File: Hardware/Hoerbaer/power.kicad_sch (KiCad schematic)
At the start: 62 parts, among them J12 Battery 1S Li-Ion, Q1 DMG3415UQ-7, U12 MAX17048G, U13 TPS61288, U8 MCP73831T-2ACI/OT (4.2V), U9 TPS63001

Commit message: Many small corrections, changed connectors, ...
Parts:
- added J10: Battery 1S Li-Ion, Connector_Wire:SolderWire-0.5sqmm_1x02_P4.6mm_D0.9mm_OD2.1mm, symbol Connector_Generic:Conn_01x02
- J12: footprint Connector_Phoenix_MSTB:PhoenixContact_MSTBVA_2,5_2-G-5,08_1x02_P5.08mm_Vertical -> Connector_JST:JST_XH_B2B-XH-AM_1x02_P2.50mm_Vertical; LCSC (none) -> C158012; MPN (none) -> B2B-XH-A(LF)(SN); now not fitted
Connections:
- net +BATT: now also J10.2 (Pin_2)
- net GND: now also J10.1 (Pin_1)
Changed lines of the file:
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@@
   (junction (at 191.77 142.24) (diameter 0) (color 0 0 0 0)
   )
+  (junction (at 237.49 139.7) (diameter 0) (color 0 0 0 0)
+  )
   (junction (at 107.95 43.18) (diameter 0) (color 0 0 0 0)
   )
@@
     (stroke (width 0) (type default))
   )
+  (wire (pts (xy 237.49 139.7) (xy 237.49 153.67))
+    (stroke (width 0) (type default))
+  )
   (wire (pts (xy 191.77 142.24) (xy 191.77 138.43))
     (stroke (width 0) (type default))
@@
     (stroke (width 0) (type default))
   )
+  (wire (pts (xy 237.49 153.67) (xy 245.11 153.67))
+    (stroke (width 0) (type default))
+  )
   (wire (pts (xy 199.39 142.24) (xy 199.39 146.05))
     (stroke (width 0) (type default))
@@
     )
   )
+  (symbol (lib_id "Connector_Generic:Conn_01x02") (at 250.19 156.21 0) (mirror x) (unit 1)
+    (in_bom no) (on_board yes) (dnp no)
+    (property "Reference" "J10" (at 252.73 156.21 0)
+      (effects (font (size 1.27 1.27)) (justify left))
+    )
+    (property "Value" "Battery 1S Li-Ion" (at 252.73 153.67 0)
+      (effects (font (size 1.27 1.27)) (justify left))
+    )
+    (property "Footprint" "Connector_Wire:SolderWire-0.5sqmm_1x02_P4.6mm_D0.9mm_OD2.1mm" (at 250.19 156.21 0)
+      (effects (font (size 1.27 1.27)) hide)
+    )
+    (property "Datasheet" "~" (at 250.19 156.21 0)
+      (effects (font (size 1.27 1.27)) hide)
+    )
+    (property "MPN" "" (at 250.19 156.21 0)
+      (effects (font (size 1.27 1.27)) hide)
+    )
+    (property "LCSC" "" (at 250.19 156.21 0)
+      (effects (font (size 1.27 1.27)) hide)
+    )
+    (property "Field6" "" (at 250.19 156.21 0)
+      (effects (font (size 1.27 1.27)) hide)
+    )
+    (pin "1")
+    (pin "2")
+    (instances
+      (project "Hoerbaer"
+        (path "/31f16f54-0469-45ae-b442-d363bf5fad3b/619abe22-66a2-4b7d-b472-86dccb0a4dd1"
+          (reference "J10") (unit 1)
+        )
+      )
+    )
+  )
   (symbol (lib_id "Connector:TestPoint") (at 181.61 43.18 270) (unit 1)
     (in_bom no) (on_board yes) (dnp no)
@@
     )
   )
+  (symbol (lib_id "power:GND") (at 245.11 156.21 0) (unit 1)
+    (in_bom yes) (on_board yes) (dnp no)
+    (property "Reference" "#PWR0193" (at 245.11 162.56 0)
+      (effects (font (size 1.27 1.27)) hide)
+    )
+    (property "Value" "GND" (at 245.11 160.02 0)
+      (effects (font (size 1.27 1.27)))
+    )
+    (property "Footprint" "" (at 245.11 156.21 0)
+      (effects (font (size 1.27 1.27)) hide)
+    )
+    (property "Datasheet" "" (at 245.11 156.21 0)
+      (effects (font (size 1.27 1.27)) hide)
+    )
+    (pin "1")
+    (instances
+      (project "Hoerbaer"
+        (path "/31f16f54-0469-45ae-b442-d363bf5fad3b/619abe22-66a2-4b7d-b472-86dccb0a4dd1"
+          (reference "#PWR0193") (unit 1)
+        )
+      )
+    )
+  )
   (symbol (lib_id "Baer_Symbols:MAX17048 DFN8") (at 247.65 102.87 0) (unit 1)
     (in_bom yes) (on_board yes) (dnp no) (fields_autoplaced)
@@
   )
   (symbol (lib_id "Connector_Generic:Conn_01x02") (at 250.19 142.24 0) (mirror x) (unit 1)
-    (in_bom yes) (on_board yes) (dnp no)
+    (in_bom yes) (on_board yes) (dnp yes)
     (property "Reference" "J12" (at 252.73 142.24 0)
       (effects (font (size 1.27 1.27)) (justify left))
@@
       (effects (font (size 1.27 1.27)) (justify left))
     )
-    (property "Footprint" "Connector_Phoenix_MSTB:PhoenixContact_MSTBVA_2,5_2-G-5,08_1x02_P5.08mm_Vertical" (at 250.19 142.24 0)
+    (property "Footprint" "Connector_JST:JST_XH_B2B-XH-AM_1x02_P2.50mm_Vertical" (at 250.19 142.24 0)
       (effects (font (size 1.27 1.27)) hide)
     )
@@
       (effects (font (size 1.27 1.27)) hide)
     )
+    (property "MPN" "B2B-XH-A(LF)(SN)" (at 250.19 142.24 0)
+      (effects (font (size 1.27 1.27)) hide)
+    )
+    (property "LCSC" "C158012" (at 250.19 142.24 0)
+      (effects (font (size 1.27 1.27)) hide)
+    )

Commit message: DRC fixes
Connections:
- net GND: now also NT1.1, NT10.1, NT11.1, NT12.1, NT13.1, NT14.1, NT2.1, NT3.1, NT4.1, NT5.1, NT6.1, NT7.1, NT8.1, NT9.1; no longer NT1.2, NT10.2, NT11.2, NT12.2, NT13.2, NT14.2, NT2.2, NT3.2, NT4.2, NT5.2, NT6.2, NT7.2, NT8.2, NT9.2
- net GNDPWR: now also NT1.2, NT10.2, NT11.2, NT12.2, NT13.2, NT14.2, NT2.2, NT3.2, NT4.2, NT5.2, NT6.2, NT7.2, NT8.2, NT9.2; no longer NT1.1, NT10.1, NT11.1, NT12.1, NT13.1, NT14.1, NT2.1, NT3.1, NT4.1, NT5.1, NT6.1, NT7.1, NT8.1, NT9.1
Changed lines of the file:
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@@
     )
   )
-  (symbol (lib_id "power:GNDPWR") (at 176.53 146.05 0) (unit 1)
+  (symbol (lib_id "power:GNDPWR") (at 184.15 146.05 0) (unit 1)
     (in_bom yes) (on_board yes) (dnp no) (fields_autoplaced)
-    (property "Reference" "#PWR0151" (at 176.53 151.13 0)
-      (effects (font (size 1.27 1.27)) hide)
-    )
-    (property "Value" "GNDPWR" (at 176.403 149.86 0)
-      (effects (font (size 1.27 1.27)))
-    )
-    (property "Footprint" "" (at 176.53 147.32 0)
-      (effects (font (size 1.27 1.27)) hide)
-    )
-    (property "Datasheet" "" (at 176.53 147.32 0)
+    (property "Reference" "#PWR0151" (at 184.15 151.13 0)
+      (effects (font (size 1.27 1.27)) hide)
+    )
+    (property "Value" "GNDPWR" (at 184.023 149.86 0)
+      (effects (font (size 1.27 1.27)))
+    )
+    (property "Footprint" "" (at 184.15 147.32 0)
+      (effects (font (size 1.27 1.27)) hide)
+    )
+    (property "Datasheet" "" (at 184.15 147.32 0)
       (effects (font (size 1.27 1.27)) hide)
     )
@@
     )
   )
-  (symbol (lib_id "power:GND") (at 184.15 146.05 0) (unit 1)
-    (in_bom yes) (on_board yes) (dnp no)
-    (property "Reference" "#PWR0152" (at 184.15 152.4 0)
-      (effects (font (size 1.27 1.27)) hide)
-    )
-    (property "Value" "GND" (at 184.15 149.86 0)
-      (effects (font (size 1.27 1.27)))
-    )
-    (property "Footprint" "" (at 184.15 146.05 0)
-      (effects (font (size 1.27 1.27)) hide)
-    )
-    (property "Datasheet" "" (at 184.15 146.05 0)
+  (symbol (lib_id "power:GND") (at 176.53 146.05 0) (unit 1)
+    (in_bom yes) (on_board yes) (dnp no)
+    (property "Reference" "#PWR0152" (at 176.53 152.4 0)
+      (effects (font (size 1.27 1.27)) hide)
+    )
+    (property "Value" "GND" (at 176.53 149.86 0)
+      (effects (font (size 1.27 1.27)))
+    )
+    (property "Footprint" "" (at 176.53 146.05 0)
+      (effects (font (size 1.27 1.27)) hide)
+    )
+    (property "Datasheet" "" (at 176.53 146.05 0)
       (effects (font (size 1.27 1.27)) hide)
     )
@@
     )
   )
-  (symbol (lib_id "power:GNDPWR") (at 191.77 146.05 0) (unit 1)
+  (symbol (lib_id "power:GNDPWR") (at 199.39 146.05 0) (unit 1)
     (in_bom yes) (on_board yes) (dnp no) (fields_autoplaced)
-    (property "Reference" "#PWR0190" (at 191.77 151.13 0)
-      (effects (font (size 1.27 1.27)) hide)
-    )
-    (property "Value" "GNDPWR" (at 191.643 149.86 0)
-      (effects (font (size 1.27 1.27)))
-    )
-    (property "Footprint" "" (at 191.77 147.32 0)
-      (effects (font (size 1.27 1.27)) hide)
-    )
-    (property "Datasheet" "" (at 191.77 147.32 0)
+    (property "Reference" "#PWR0190" (at 199.39 151.13 0)
+      (effects (font (size 1.27 1.27)) hide)
+    )
+    (property "Value" "GNDPWR" (at 199.263 149.86 0)
+      (effects (font (size 1.27 1.27)))
+    )
+    (property "Footprint" "" (at 199.39 147.32 0)
+      (effects (font (size 1.27 1.27)) hide)
+    )
+    (property "Datasheet" "" (at 199.39 147.32 0)
       (effects (font (size 1.27 1.27)) hide)
     )
@@
     )
   )
-  (symbol (lib_id "power:GND") (at 199.39 146.05 0) (unit 1)
-    (in_bom yes) (on_board yes) (dnp no)
-    (property "Reference" "#PWR0191" (at 199.39 152.4 0)
-      (effects (font (size 1.27 1.27)) hide)
-    )
-    (property "Value" "GND" (at 199.39 149.86 0)
-      (effects (font (size 1.27 1.27)))
-    )
-    (property "Footprint" "" (at 199.39 146.05 0)
-      (effects (font (size 1.27 1.27)) hide)
-    )
-    (property "Datasheet" "" (at 199.39 146.05 0)
-      (effects (font (size 1.27 1.27)) hide)
-    )
+  (symbol (lib_id "power:GND") (at 191.77 146.05 0) (unit 1)
+    (in_bom yes) (on_board yes) (dnp no)
+    (property "Reference" "#PWR0191" (at 191.77 152.4 0)
+      (effects (font (size 1.27 1.27)) hide)
+    )
+    (property "Value" "GND" (at 191.77 149.86 0)
+      (effects (font (size 1.27 1.27)))
+    )
+    (property "Footprint" "" (at 191.77 146.05 0)
+      (effects (font (size 1.27 1.27)) hide)
+    )
+    (property "Datasheet" "" (at 191.77 146.05 0)
+      (effects (font (size 1.27 1.27)) hide)
+    )

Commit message: Fixed 1uF order number.
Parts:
- C15, C20: LCSC C726581 -> C29266; MPN AC0805KKX7R6BB105 -> CL05A105KO5NNNC
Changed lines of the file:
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@@
       (effects (font (size 1.27 1.27)) hide)
     )
-    (property "LCSC" "C726581" (at 181.61 48.26 0)
-      (effects (font (size 1.27 1.27)) hide)
-    )
-    (property "MPN" "AC0805KKX7R6BB105" (at 181.61 48.26 0)
+    (property "LCSC" "C29266 " (at 181.61 48.26 0)
+      (effects (font (size 1.27 1.27)) hide)
+    )
+    (property "MPN" "CL05A105KO5NNNC" (at 181.61 48.26 0)
       (effects (font (size 1.27 1.27)) hide)
     )
@@
       (effects (font (size 1.27 1.27)) hide)
     )
-    (property "LCSC" "C726581" (at 121.92 123.19 0)
-      (effects (font (size 1.27 1.27)) hide)
-    )
-    (property "MPN" "AC0805KKX7R6BB105" (at 121.92 123.19 0)
-      (effects (font (size 1.27 1.27)) hide)
-    )
+    (property "LCSC" "C29266 " (at 121.92 123.19 0)
+      (effects (font (size 1.27 1.27)) hide)
+    )
+    (property "MPN" "CL05A105KO5NNNC" (at 121.92 123.19 0)
+      (effects (font (size 1.27 1.27)) hide)
+    )

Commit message: WIP new hw rev
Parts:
- removed C44 (x3): 22µF, low ESR, Capacitor_SMD:C_1210_3225Metric, symbol Device:C_Small
- removed C55: 4.7µF, 10V, Capacitor_SMD:C_0805_2012Metric, symbol Device:C_Small
- removed C62: 47µF, Capacitor_SMD:CP_Elec_6.3x5.9, symbol Device:C_Polarized_Small
- removed NT10, NT11, NT2, NT5, NT6, NT9: GNDs, Baer_Footprints:NetTie-2_Via, symbol Device:NetTie_2
- removed Q1: DMG3415UQ-7, Package_TO_SOT_SMD:SOT-23, symbol Device:Q_PMOS_GSD
- removed R11: 10kΩ, Resistor_SMD:R_0402_1005Metric, symbol Device:R_Small
- removed R11: 100kΩ, Resistor_SMD:R_0402_1005Metric, symbol Device:R_Small
- removed R62: 2kΩ, Resistor_SMD:R_0402_1005Metric, symbol Device:R_Small
- removed U8: MCP73831T-2ACI/OT (4.2V), Package_TO_SOT_SMD:SOT-23-5, symbol Baer_Symbols:MCP73831/2_SOT
- added C19: 1µF, 16V, Capacitor_SMD:C_0402_1005Metric, symbol Device:C_Small
- added C20: 10µF, Capacitor_SMD:C_0805_2012Metric, symbol Device:C_Small
- added C33, C34: 100nF, Capacitor_SMD:C_0402_1005Metric, symbol Device:C_Small
- added D11, D5: S54BF, Baer_Footprints:S54BF, symbol Device:D_Schottky
- added D12: LESD5D5.0CT1G, Diode_SMD:D_SOD-523, symbol Device:D_TVS
- added D4: YELLOW, LED_SMD:LED_0603_1608Metric, symbol Device:LED
- added D6: GREEN, LED_SMD:LED_0603_1608Metric, symbol Device:LED
- added J12: VExt 5V, Connector_Wire:SolderWire-0.5sqmm_1x02_P4.6mm_D0.9mm_OD2.1mm, symbol Connector_Generic:Conn_01x02
- added J13: TS, Connector_PinHeader_2.54mm:PinHeader_1x02_P2.54mm_Vertical, symbol Connector_Generic:Conn_01x02
- added JP1: EN2, Jumper:SolderJumper-3_P1.3mm_Bridged12_RoundedPad1.0x1.5mm, symbol Jumper:SolderJumper_3_Bridged12
- added JP10: V, Jumper:SolderJumper-3_P1.3mm_Bridged12_RoundedPad1.0x1.5mm, symbol Jumper:SolderJumper_3_Bridged12
- added JP2: EN1, Jumper:SolderJumper-3_P1.3mm_Bridged12_RoundedPad1.0x1.5mm, symbol Jumper:SolderJumper_3_Bridged12
- added JP3: TD, Jumper:SolderJumper-3_P1.3mm_Bridged12_RoundedPad1.0x1.5mm, symbol Jumper:SolderJumper_3_Bridged12
- added JP4: TMR, Jumper:SolderJumper-2_P1.3mm_Open_RoundedPad1.0x1.5mm, symbol Jumper:SolderJumper_2_Open
- added JP5: FIX_TS, Jumper:SolderJumper-2_P1.3mm_Open_RoundedPad1.0x1.5mm, symbol Jumper:SolderJumper_2_Open
- added R49, R51: 5.1kΩ, Resistor_SMD:R_0402_1005Metric, symbol Device:R_Small
- added R50, R52: 1.13kΩ, Resistor_SMD:R_0402_1005Metric, symbol Device:R_Small
- added R53, R70: 10kΩ, Resistor_SMD:R_0402_1005Metric, symbol Device:R_Small
- added R68: 90kΩ, Resistor_SMD:R_0402_1005Metric, symbol Device:R_Small
- added R69: 100Ω, Resistor_SMD:R_0402_1005Metric, symbol Device:R_Small
- added TP10: VCC_P_EN, TestPoint:TestPoint_Pad_D1.5mm, symbol Connector:TestPoint
- added TP5: CHG_PGOOD, TestPoint:TestPoint_Pad_D1.5mm, symbol Connector:TestPoint
- added TP7: SW_VIN, TestPoint:TestPoint_Pad_D1.5mm, symbol Connector:TestPoint
- added U14: TPS22810DRV, Package_SON:WSON-6-1EP_2x2mm_P0.65mm_EP1x1.6mm_ThermalVias, symbol Power_Management:TPS22810DRV
- added U8: BQ24073RGT, Package_DFN_QFN:VQFN-16-1EP_3x3mm_P0.5mm_EP1.6x1.6mm, symbol Battery_Management:BQ24073RGT
- C27: renamed from C20; value 1µF, 10V -> 1µF, 16V; LCSC C29266 -> C29266
- C35: renamed from C15; value 1µF, 10V -> 1µF, 16V; LCSC C29266 -> C29266
- L1: renamed from L2; value 4.7uH, 14A -> 5.6uH, 3.85A; footprint Baer_Footprints:L_TDK_SPM12565 -> Inductor_SMD:L_Sunlord_SWPA8040S; LCSC C2048059 -> C96972; MPN SPM12565VT-4R7M-D Copy -> SWPA8040S5R6NT
- R55: renamed from R53; value 191kΩ -> 140kΩ; LCSC C270632 -> C114151; MPN 0402WGF1913TCE -> RC0402FR-07140KL
- TP2: renamed from TP7; value 12V_EN -> 9V_EN
- TP9: renamed from TP10; value +12V -> +9V
- renumbered C19 to C18, C55 to C21, C13 to C22, C26 to C23, C25 to C24, C12 to C25, C21 to C26, C14 to C28, C60 to C29, C59 to C30, C61 to C31, C16 to C32, C44 to C37, C44 to C38, C44 to C39, D3 to D7, J12 to J14, J10 to J15, L1 to L2, R11 to R46, R11 to R47, R11 to R48, R11 to R54, R54 to R56, R55 to R57, TP6 to TP1, TP9 to TP3, TP8 to TP4, TP5 to TP6, TP4 to TP8, U9 to U10, U13 to U11, U12 to U9
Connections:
- net +BATT: now also U8.2 (BAT), U8.3 (BAT)
- net CHG_STAT: now also D4.1 (K), U8.9 (~{CHG})
- net GND: now also C19.2, C20.2, C33.2, C34.2, D12.1 (A1), J12.1 (Pin_1), J13.1 (Pin_1), JP1.3 (B), JP2.1 (A), JP3.1 (A), JP4.1 (A), R50.2, R52.2, R53.2, R70.2, U14.4 (GND), U14.7 (GND), U8.17 (VSS), U8.4 (~{CE}), U8.8 (VSS)
- net SWITCHER_VIN: now also C20.1, JP1.1 (A), JP2.3 (B), JP3.3 (B), TP7.1, U8.10 (OUT), U8.11 (OUT); no longer D7.1 (K)
- net VBUS: now also D5.2 (A); no longer D7.2 (A)
- net VCC: now also C33.1, R49.1, R51.1, U14.6 (VIN)
- net at C30.1, R56.1, U11.1 (FB): now also JP10.2 (C); no longer R55.2
- net +12V renamed +9V
- net +9V: now also R68.1
- net 12V_EN renamed 9V_EN
- net 12V_SW renamed 9V_SW
- new net: R69.2, U14.2 (QOD)
- new net: D12.2 (A2), D7.2 (A), J12.2 (Pin_2)
- new net: C19.1, D11.1 (K), D5.1 (K), D7.1 (K), U8.13 (IN)
- new net: R52.1, U8.16 (ISET)
- new net: JP10.1 (A), R55.2
- new net: JP4.2 (B), U8.14 (TMR)
- new net: JP2.2 (C), U8.6 (EN1)
- new net: C34.1, U14.3 (CT)
- new net: R50.1, U8.12 (ILIM)
- new net: JP3.2 (C), U8.15 (TD)
- new net: JP1.2 (C), U8.5 (EN2)
- new net: JP10.3 (B), R68.2
- new net: D4.2 (A), R49.2
- new net: D6.2 (A), R51.2
- new net: JP5.1 (A), R53.1
- new net CHG_PGOOD: D6.1 (K), TP5.1, U8.7 (~{PGOOD})
- new net CHG_TS: J13.2 (Pin_2), JP5.2 (B), U8.1 (TS)
- new net VBUS_USB2: D11.2 (A)
- new net VCC_P: R69.1, U14.1 (VOUT)
- new net VCC_P_EN: R70.1, TP10.1, U14.5 (EN/UVLO)
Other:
- note added: "10kΩ NTC thermistor. Unused: Connect a 10-kΩ fixed resistor from TS to VSS to maintain a valid voltage level on TS."
- note added: "9V (Boost)"
- note added: "BQ24073RGT Config Pins EN2 EN1 0 0 100 mA. USB100 mode 0 1 500 mA. USB500 mode 1 0 Set by R ILIM to VSS 1 1 Standby (USB suspend mode) TMR flaoting: default safety timer values TMR GND: timer disabled TD low: Termination enabled TD high: Termination disabled"
- note added: "BQ24073RGT Current settings TGT: ISET = 0.8A (Imax fast chg), ILIM = 1.4A (Imax Input) R_{ISET} = 890 AΩ / 0.8 A = 1.1125 kΩ => 1.13kΩ R_{ILIM} = 1550 AΩ / 1.4 A = 1.1107 kΩ => 1.13kΩ"
- note added: "Battery Connector"
- note added: "Battery Thermistor"
- note added: "Charger / PowerPath"
- note removed: "12V (Boost)"
- note removed: "Charger"
- note removed: "Connector"
- note removed: "R_{PROG} - DS 5.1.2 p.15 IREG = 1000V / R_{PROG} = 500mA (@2kΩ) 6 hours full charge for one 3000mAh 18650 Li-Ion Cell"
- moved on the sheet: C18, C21, C22, C23, C24, C25, C26, C27, C28, C29, C30, C31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

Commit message: Layout, mono-jumpers
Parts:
- added TP11: VBUS, TestPoint:TestPoint_Pad_D1.5mm, symbol Connector:TestPoint
- added TP12: VBUS_USB2, TestPoint:TestPoint_Pad_D1.5mm, symbol Connector:TestPoint
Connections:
- net SWITCHER_VIN: now also R49.1, R51.1
- net VBUS: now also TP11.1
- net VBUS_USB2: now also TP12.1
- net VCC: no longer R48.1, R49.1, R51.1
- net VCC_P: now also R48.1
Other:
- moved on the sheet: D4, D6, R49, R51

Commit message: Layout rev 2 - without silkscreen
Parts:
- removed TP11: VBUS, TestPoint:TestPoint_Pad_D1.5mm, symbol Connector:TestPoint
- removed TP12: VBUS_USB2, TestPoint:TestPoint_Pad_D1.5mm, symbol Connector:TestPoint
- removed TP6: VBAT, TestPoint:TestPoint_Pad_D1.5mm, symbol Connector:TestPoint

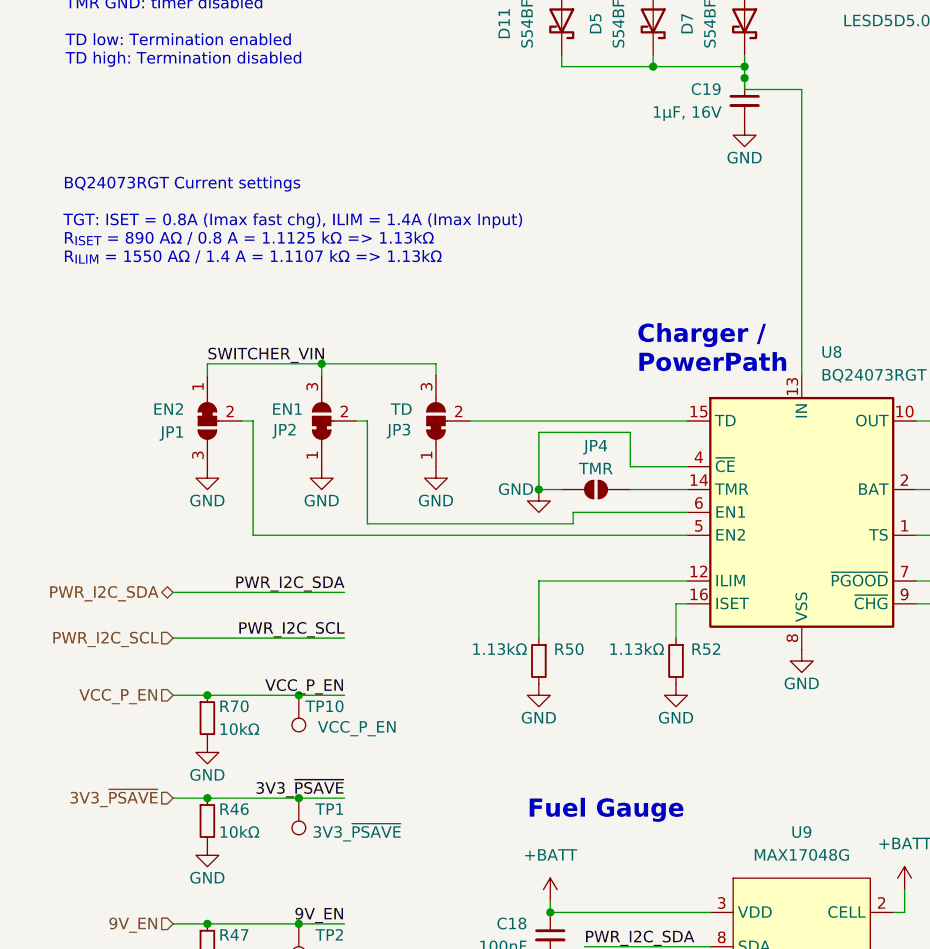
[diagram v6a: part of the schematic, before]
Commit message: Added more jumper options.
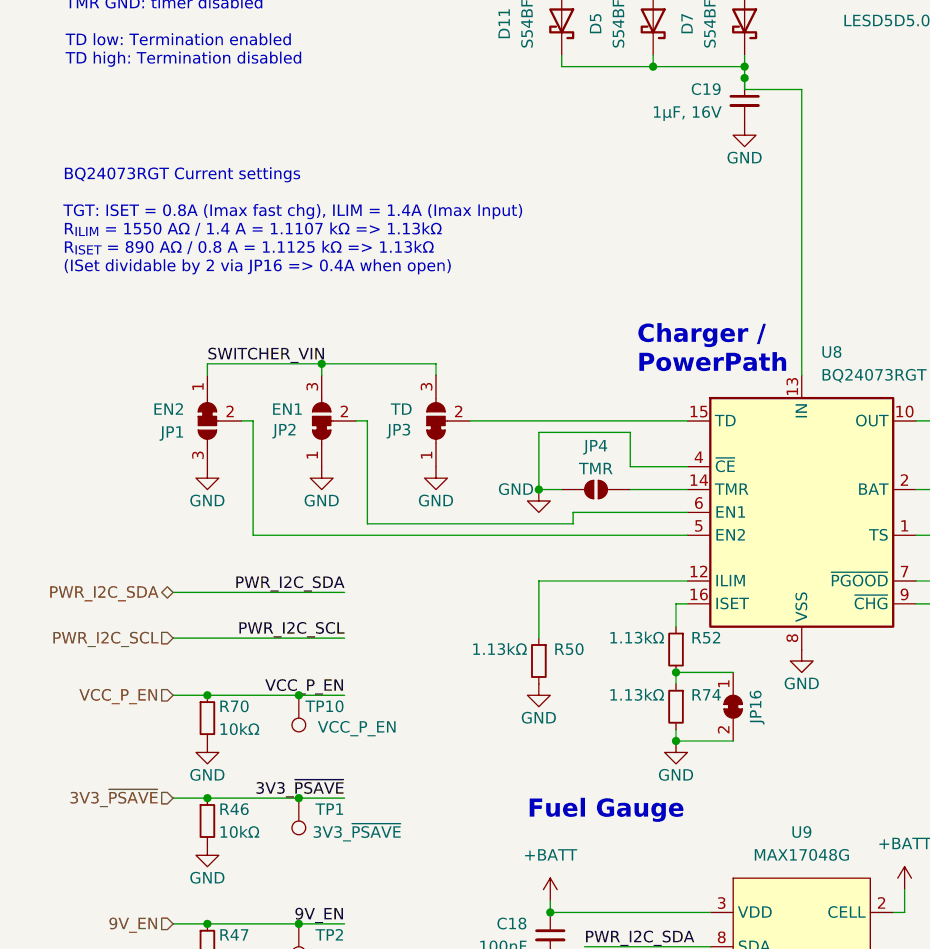
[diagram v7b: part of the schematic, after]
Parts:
- added JP16: ~{RST}, Jumper:SolderJumper-2_P1.3mm_Bridged_RoundedPad1.0x1.5mm, symbol Jumper:SolderJumper_2_Bridged
- added R74: 1.13kΩ, Resistor_SMD:R_0402_1005Metric, symbol Device:R_Small
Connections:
- net GND: now also JP16.2 (B), R74.2; no longer R52.2
- new net: JP16.1 (A), R52.2, R74.1
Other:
- note added: "BQ24073RGT Current settings TGT: ISET = 0.8A (Imax fast chg), ILIM = 1.4A (Imax Input) R_{ILIM} = 1550 AΩ / 1.4 A = 1.1107 kΩ => 1.13kΩ R_{ISET} = 890 AΩ / 0.8 A = 1.1125 kΩ => 1.13kΩ (ISet dividable by 2 via JP16 => 0.4A when open)"
- note removed: "BQ24073RGT Current settings TGT: ISET = 0.8A (Imax fast chg), ILIM = 1.4A (Imax Input) R_{ISET} = 890 AΩ / 0.8 A = 1.1125 kΩ => 1.13kΩ R_{ILIM} = 1550 AΩ / 1.4 A = 1.1107 kΩ => 1.13kΩ"
- moved on the sheet: R52
